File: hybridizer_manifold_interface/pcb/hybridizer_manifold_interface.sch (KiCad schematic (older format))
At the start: 60 parts, among them P1 HEADER_02X08_SMD, P2 HEADER_02X05_SMD, U1 HALL_DRV5053, U10 MAX4215, U11 HALL_DRV5053, U12 MAX4215, U13 HALL_DRV5053, U14 MAX4215, U2 MAX4215, U3 HALL_DRV5053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

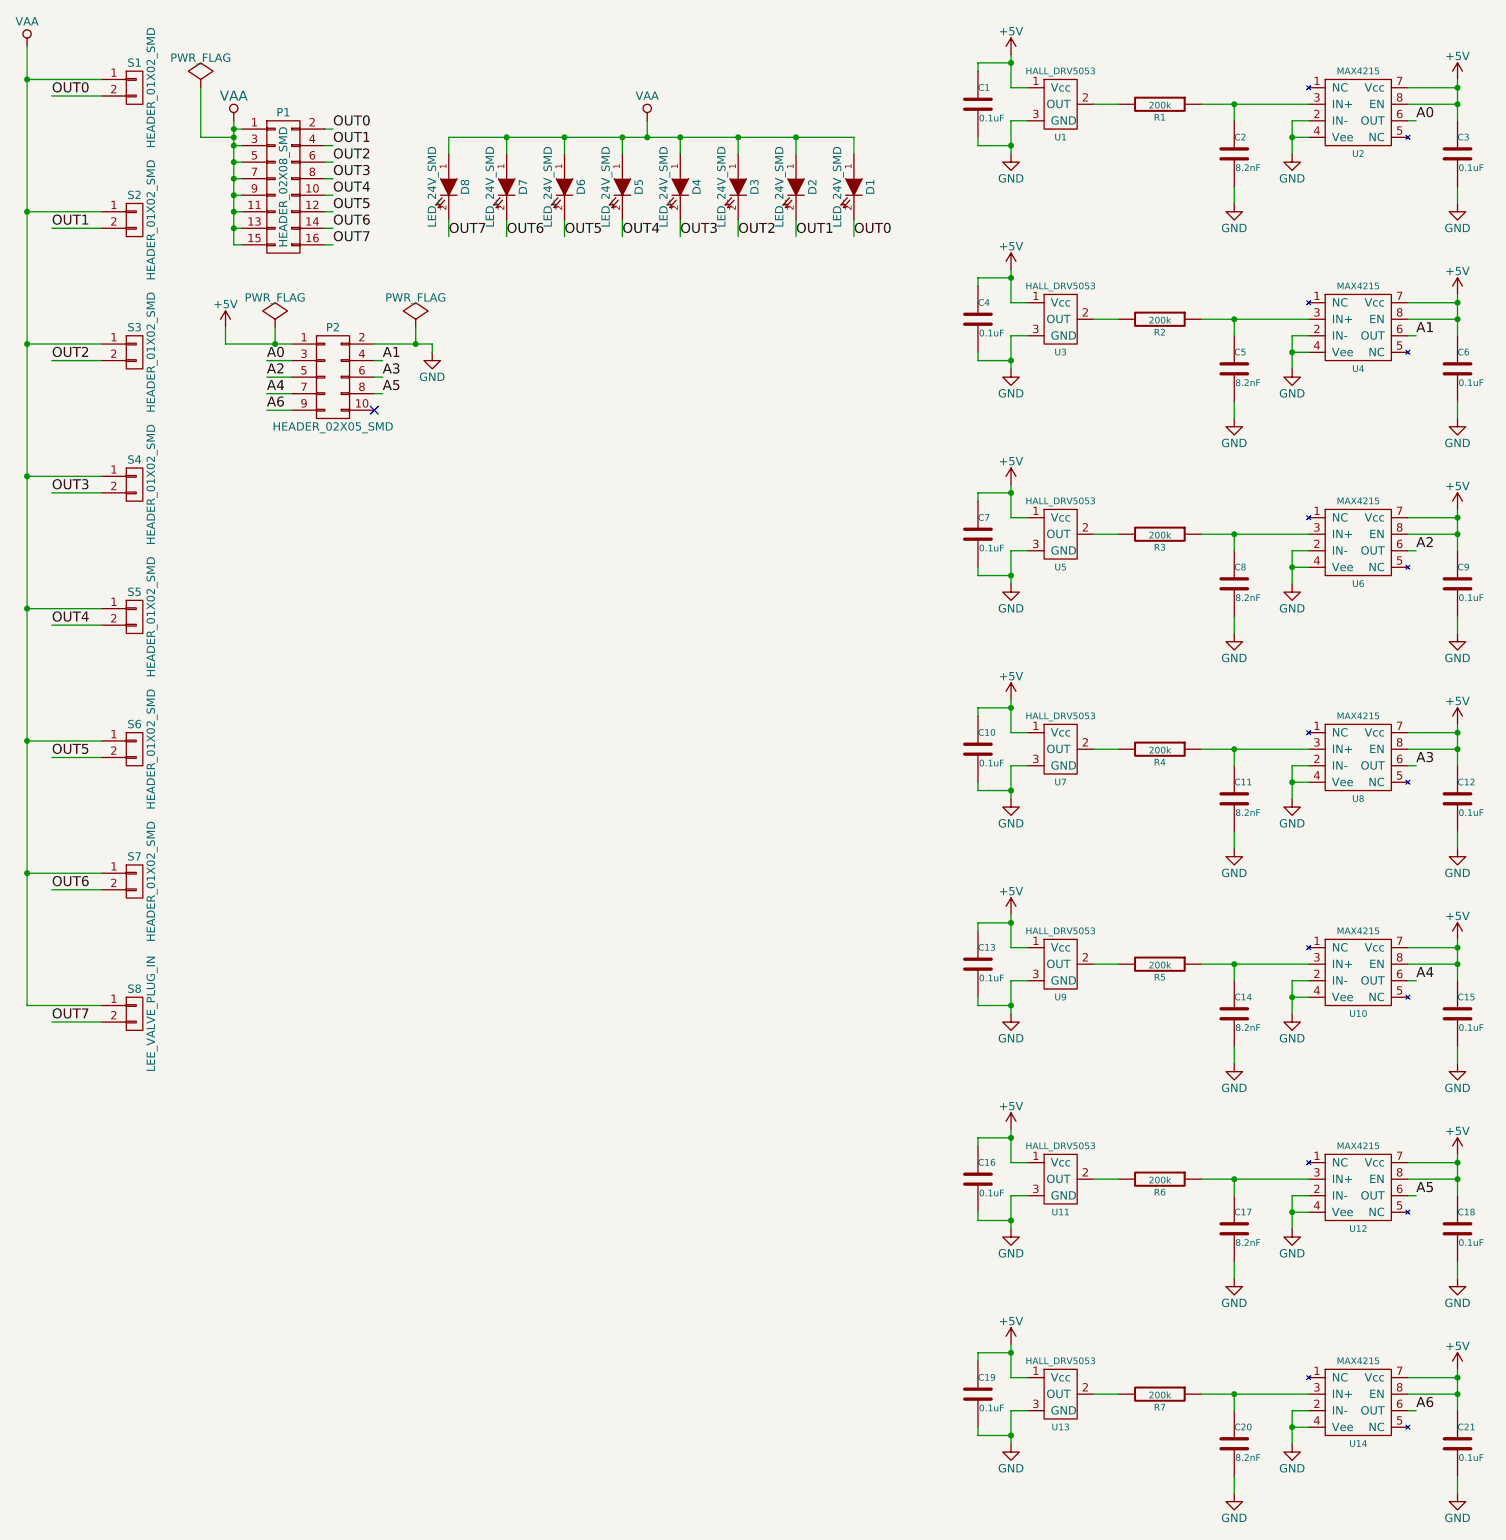
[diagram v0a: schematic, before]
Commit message: Pcb design mostly finished.
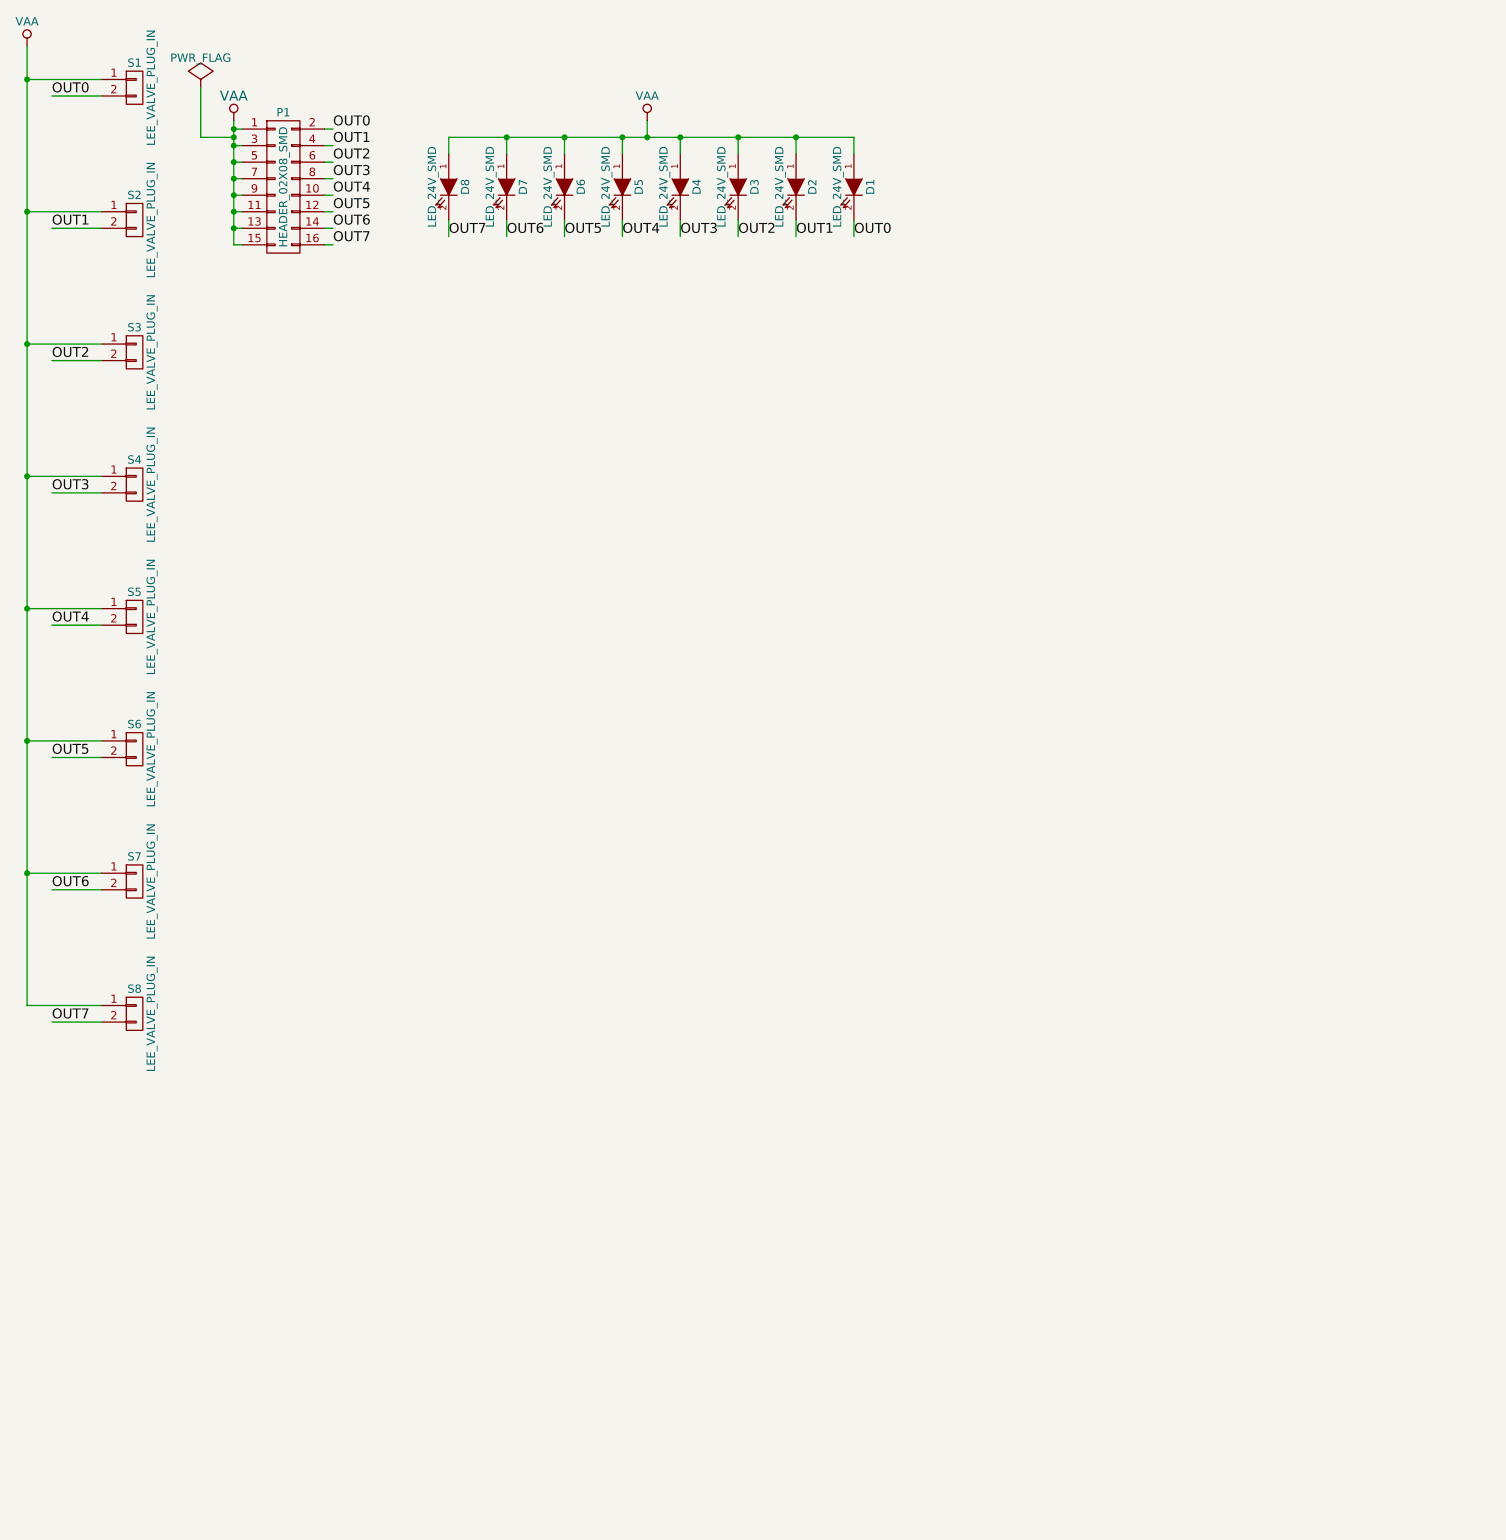
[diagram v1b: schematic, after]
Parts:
- removed C1, C10, C12, C13, C15, C16, C18, C19, C21, C3, C4, C6, C7, C9: 0.1uF, hybridizer_manifold_interface:SM1210, symbol 0.1uF
- removed C11, C14, C17, C2, C20, C5, C8: 8.2nF, hybridizer_manifold_interface:SM1210, symbol 8.2nF
- removed P2: HEADER_02X05_SMD, hybridizer_manifold_interface:HEADER_02x05_SMD, symbol HEADER_02X05_SMD
- removed R1, R2, R3, R4, R5, R6, R7: 200k, hybridizer_manifold_interface:SM1210, symbol 200k
- removed S1, S2, S3, S4, S5, S6, S7: HEADER_01X02_SMD, hybridizer_manifold_interface:Header_2_Pin_SMD, symbol HEADER_01X02_SMD
- removed U1, U11, U13, U3, U5, U7, U9: HALL_DRV5053, hybridizer_manifold_interface:SOT-23-3, symbol HALL_DRV5053
- removed U10, U12, U14, U2, U4, U6, U8: MAX4215, hybridizer_manifold_interface:SOIC_8_N, symbol MAX4215
- added S1, S2, S3, S4, S5, S6, S7: LEE_VALVE_PLUG_IN, hybridizer_manifold_interface:LEE_VALVE_PLUG_IN, symbol LEE_VALVE_PLUG_IN
- S8: Description 3 way HDI Plug In -> CONN RCPT PIN .025-.037in SOLDER
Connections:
- net OUT0: now also S1.2 (P2)
- net OUT1: now also S2.2 (P2)
- net OUT2: now also S3.2 (P2)
- net OUT3: now also S4.2 (P2)
- net OUT4: now also S5.2 (P2)
- net OUT5: now also S6.2 (P2)
- net OUT6: now also S7.2 (P2)
- net VAA: now also S1.1 (P1), S2.1 (P1), S3.1 (P1), S4.1 (P1), S5.1 (P1), S6.1 (P1), S7.1 (P1)
- no-connect marks 1 -> 0
